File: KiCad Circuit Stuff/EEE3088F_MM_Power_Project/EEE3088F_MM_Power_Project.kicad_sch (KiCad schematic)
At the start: 83 parts, among them J1 Conn_02x16_Odd_Even, J2 Conn_01x02, U1 MT3608, U11 SS-12D06-G050, U2 AMS1117-3.3, U3 TP4056, U4 INA219AIDCNR, U4 TYPE-C_16P_QTGM027, U5 HUSB237-AA001-DN06R, U6 TS5A3159DCKR, U7 AP22814AW5-7, U7 TPS5430DDAR

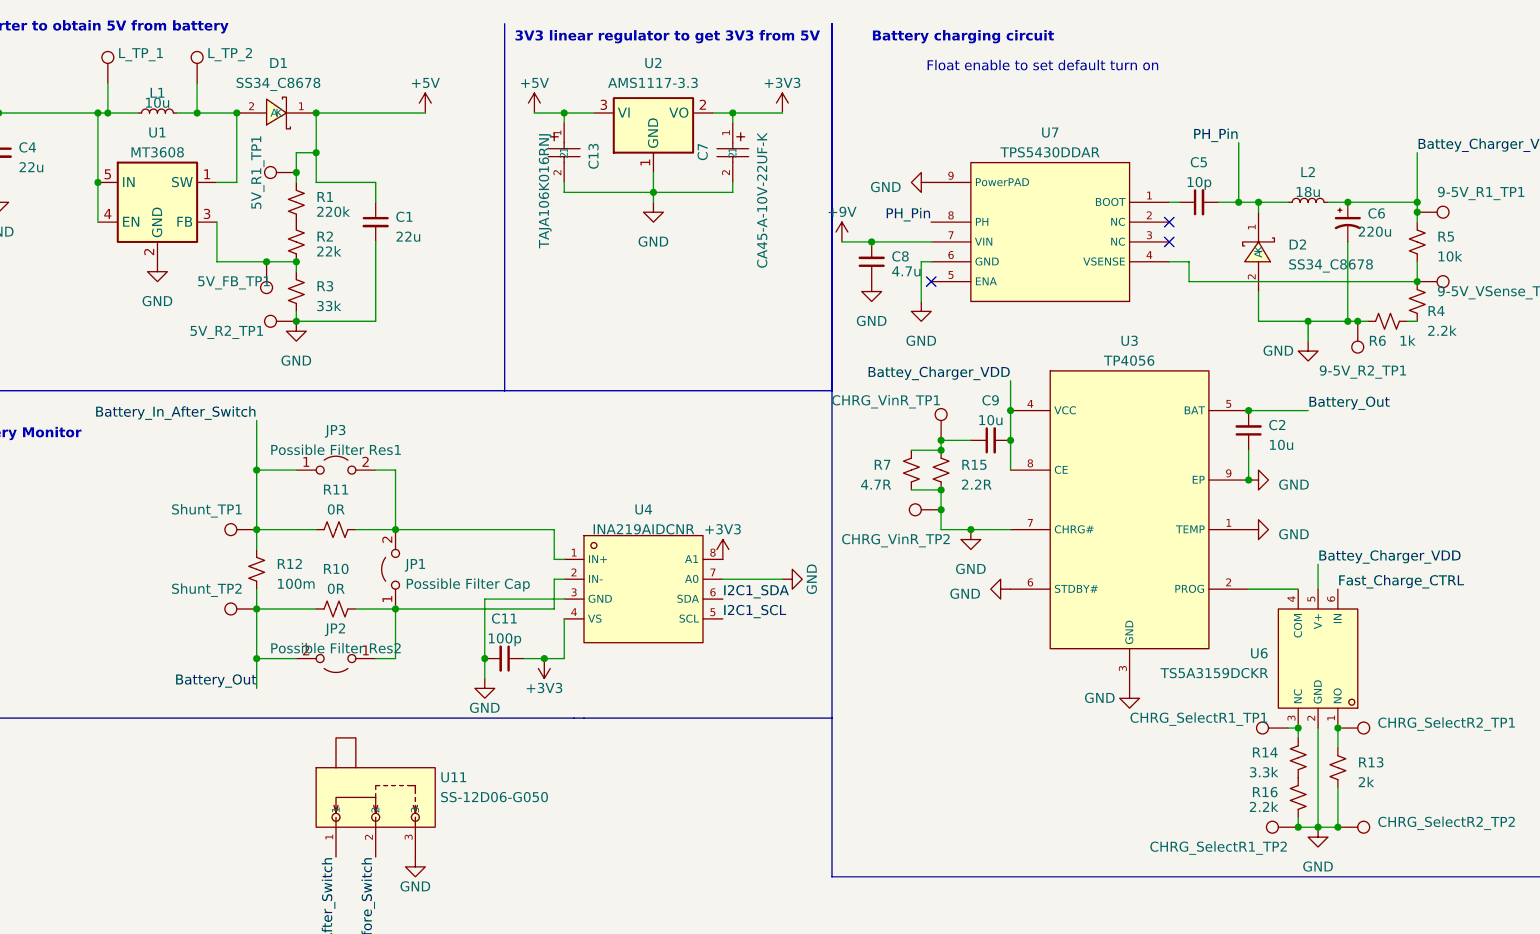
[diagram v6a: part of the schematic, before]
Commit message: Changed inductors and rewired
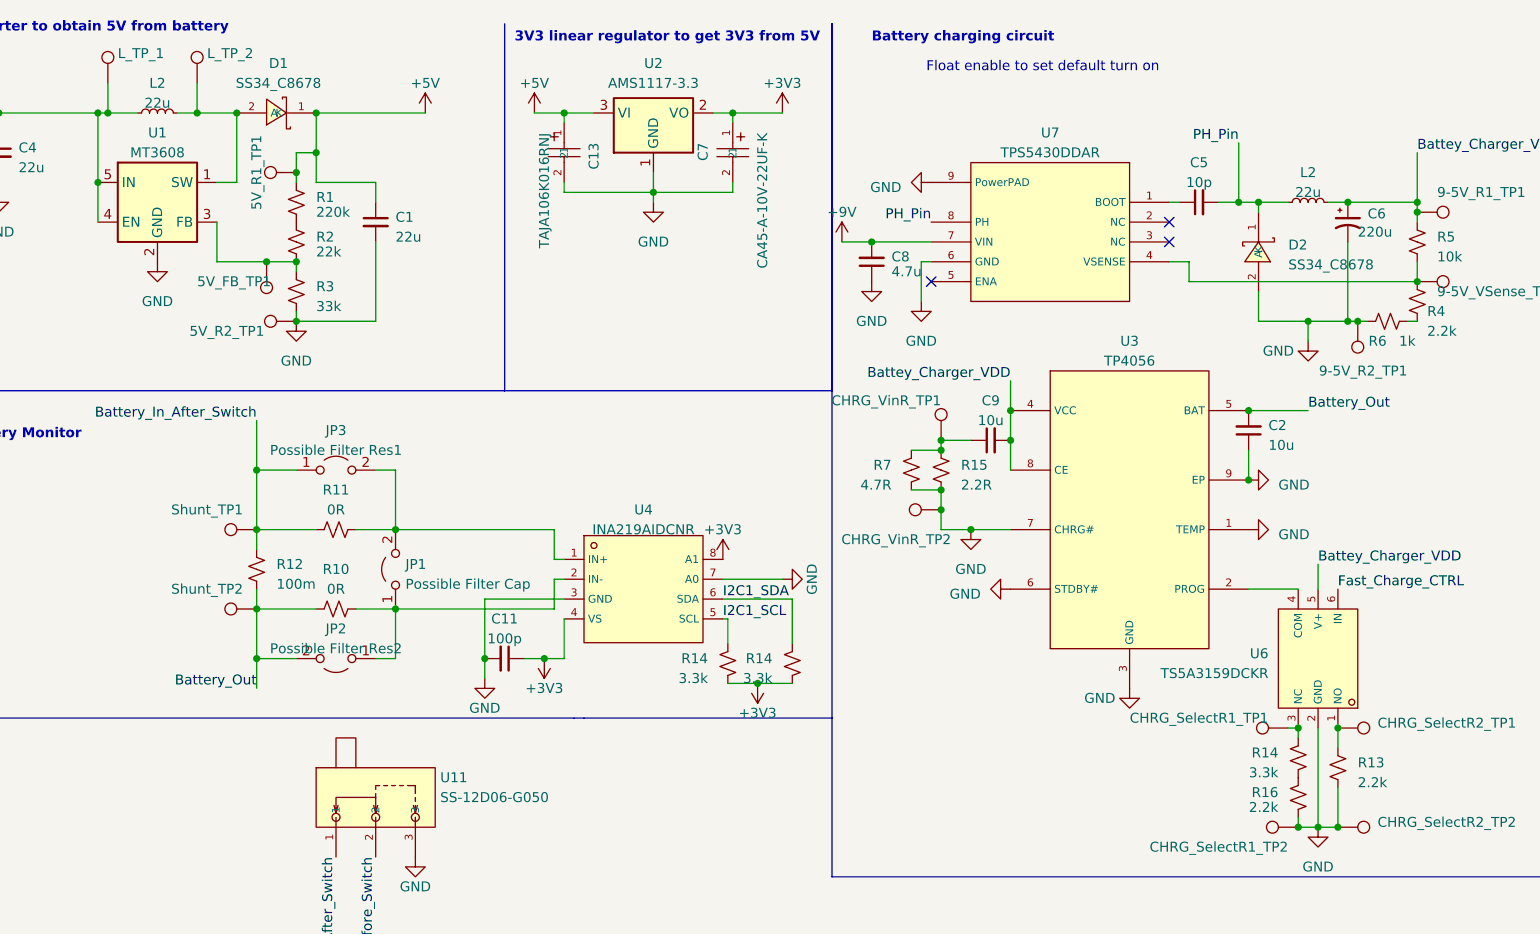
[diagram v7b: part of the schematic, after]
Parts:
- removed L1: 10u, Inductor_SMD:L_Changjiang_FNR4030S, symbol Device:L_Small
- removed L2: 18u, Inductor_SMD:L_Changjiang_FNR4030S, symbol Device:L_Small
- added L2 (x2): 22u, Inductor_SMD:L_Sunlord_SWPA6045S, symbol Device:L_Small
- added R14 (x2): 3.3k, Resistor_SMD:R_0402_1005Metric_Pad0.72x0.64mm_HandSolder, symbol Device:R_Small_US
- R13: value 2k -> 2.2k; LCSC C4109 -> C25879
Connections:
- net +3V3: now also R14.2, R14.2
- net Battery_Out: now also L2.1
- net Battey_Charger_VDD: now also L2.2
- net I2C1_SCL: now also R14.1
- net I2C1_SDA: now also R14.1
- net PH_Pin: now also L2.1
- net at D1.2 (A), L_TP_2.1, U1.1 (SW): now also L2.2

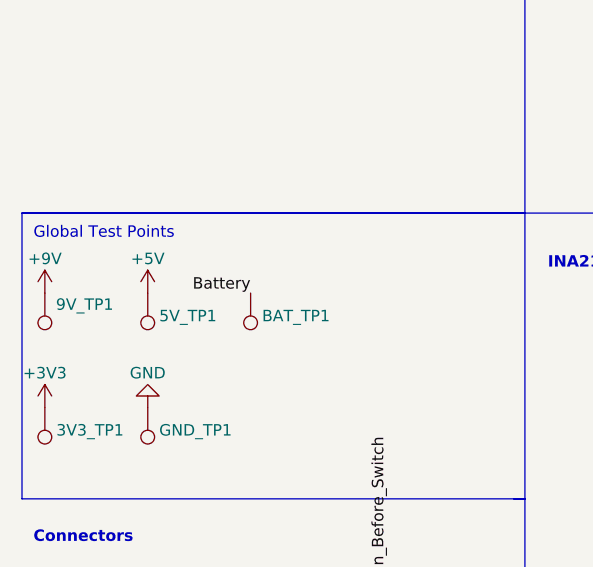
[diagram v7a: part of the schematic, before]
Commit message: Added most of all connections and holes
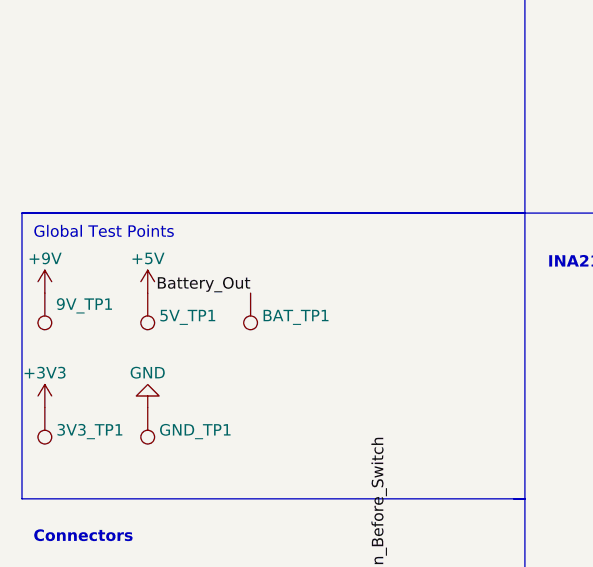
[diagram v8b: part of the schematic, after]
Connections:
- net Battery is gone; now on net Battery_Out: BAT_TP1.1
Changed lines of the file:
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@@
     (effects (font (size 0.5 0.5)) (justify right bottom))
   )
-  (label "Battery" (at 38.1 68.58 180) (fields_autoplaced)
+  (label "Battery_Out" (at 38.1 68.58 180) (fields_autoplaced)
     (effects (font (size 1.27 1.27)) (justify right bottom))
   )
